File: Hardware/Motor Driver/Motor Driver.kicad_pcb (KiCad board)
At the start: 2 copper layers, 65 x 85 mm, 9 parts, among them J1 Conn_01x02, J2 Conn_01x02, J3 Conn_01x04, J4 Conn_01x04, J5 Conn_01x06, J6 Conn_01x06, J7 Conn_01x02

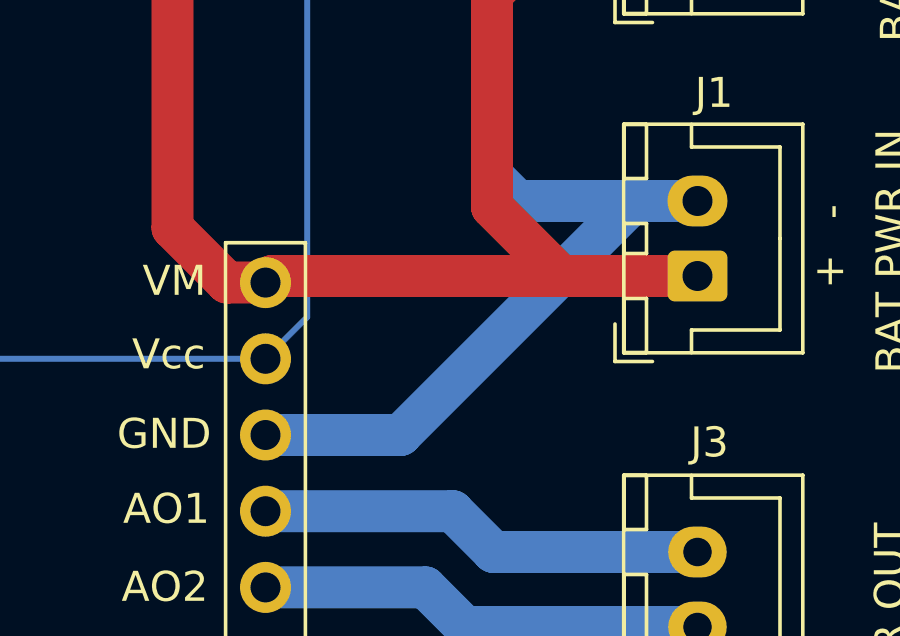
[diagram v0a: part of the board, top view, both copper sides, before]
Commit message: Updated battery input traces on the PCB.
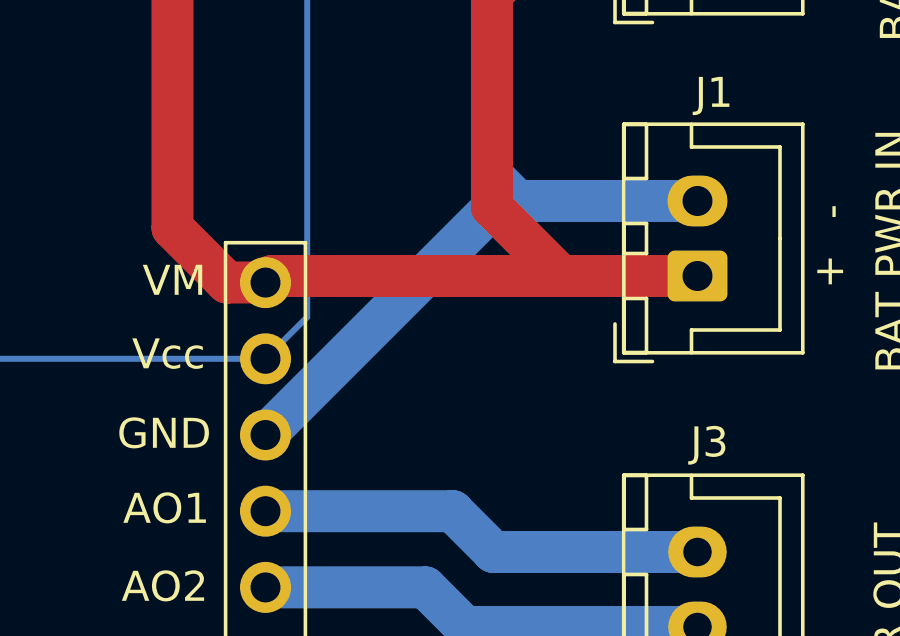
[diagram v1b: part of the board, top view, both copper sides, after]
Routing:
- net Net-(J1-Pin_2): track 71.3 -> 67.4 mm
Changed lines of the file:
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@@
+	)
+	(segment
+		(start 149.1 101.5)
+		(end 148.5 101.5)
+		(width 1.4)
+		(layer "B.Cu")
+		(net 2)
 	)
 	(segment
@@
 	(segment
 		(start 153 101.5)
-		(end 145.2 109.3)
-		(width 1.4)
-		(layer "B.Cu")
-		(net 2)
-	)
-	(segment
-		(start 153 101.5)
 		(end 149.1 101.5)
 		(width 1.4)
@@
 	)
 	(segment
-		(start 145.2 109.3)
+		(start 148.5 101.5)
 		(end 140.7 109.3)
 		(width 1.4)

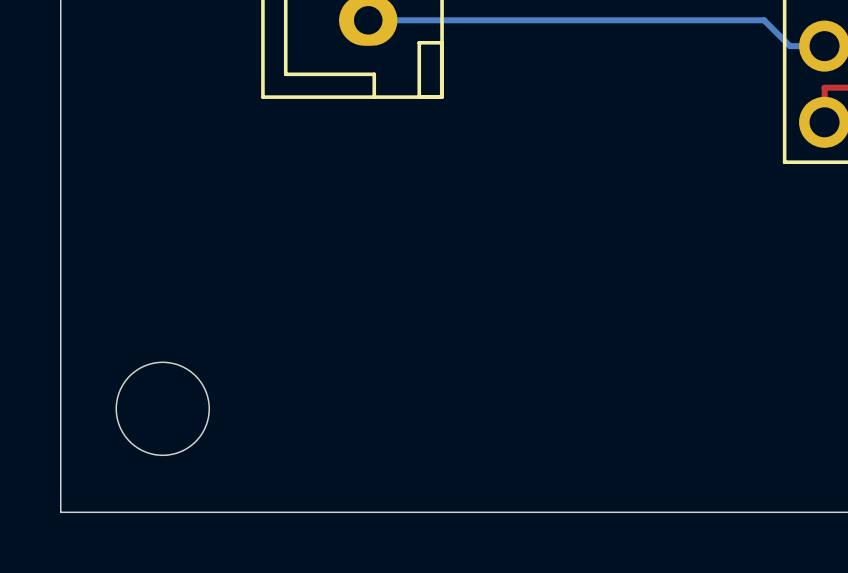
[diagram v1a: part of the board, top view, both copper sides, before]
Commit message: Added 86 logo to the front silkscreen, and designed by on the back silkscreen.
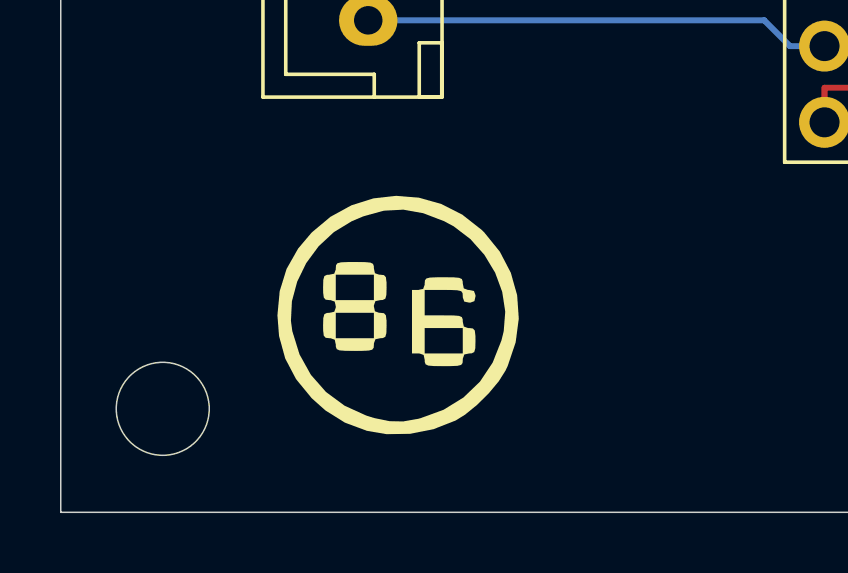
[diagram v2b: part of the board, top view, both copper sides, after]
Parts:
- added G***: LOGO, motor driver:86Carrera_logo, F.Cu at (111.2, 128.3)
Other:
- board text added: "Designed by 86 Carrera"
- board text added: "https://github.com/rallen911/Mecanum-Robot.git"
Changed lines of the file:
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@@
+		)
+	)
+	(footprint "motor driver:86Carrera_logo"
+		(layer "F.Cu")
+		(at 111.2 128.35)
+		(property "Reference" "G***"
+			(at 0 0 0)
+			(layer "F.SilkS")
+			(hide yes)
+			(effects
+				(font
+					(size 1.5 1.5)
+					(thickness 0.3)
+				)
+			)
+		)
+		(property "Value" "LOGO"
+			(at 0.75 0 0)
+			(layer "F.SilkS")
+			(hide yes)
+			(effects
+				(font
+					(size 1.5 1.5)
+					(thickness 0.3)
+				)
+			)
+		)
+		(property "Footprint" "motor driver:86Carrera_logo"
+			(at 0 0 0)
+			(layer "F.Fab")
+			(hide yes)
+			(effects
+				(font
+					(size 1.27 1.27)
+					(thickness 0.15)
+				)
+			)
+		)
+		(property "Datasheet" ""
+			(at 0 0 0)
+			(layer "F.Fab")
+			(hide yes)
+			(effects
+				(font
+					(size 1.27 1.27)
+					(thickness 0.15)
+				)
+			)
+		)
+		(property "Description" ""
+			(at 0 0 0)
+			(layer "F.Fab")
+			(hide yes)
+			(effects
+				(font
+					(size 1.27 1.27)
+					(thickness 0.15)
+				)
+			)
+		)
+		(attr board_only exclude_from_pos_files exclude_from_bom)
+		(fp_poly
+			(pts
+				(xy 0.741449 -3.837598) (xy 1.482138 -3.62887) (xy 2.183203 -3.273207) (xy 2.824011 -2.77061) (xy 2.918917 -2.677222)
+				(xy 3.435795 -2.039142) (xy 3.801361 -1.337024) (xy 4.012987 -0.587865) (xy 4.068047 0.19134) (xy 3.963912 0.983595)
+				(xy 3.697956 1.771902) (xy 3.629392 1.918851) (xy 3.39942 2.285007) (xy 3.066468 2.684218) (xy 2.676966 3.069849)
+				(xy 2.277342 3.395264) (xy 1.96754 3.588093) (xy 1.225425 3.879931) (xy 0.443616 4.033875) (xy -0.337761 4.045246)
+				(xy -0.993602 3.933478) (xy -1.726458 3.660945) (xy -2.378504 3.253211) (xy -2.83425 2.846555) (xy -3.355997 2.211121)
+				(xy -3.717833 1.522776) (xy -3.923203 0.773189) (xy -3.962943 0.267619) (xy -3.52724 0.267619) (xy -3.480628 0.613609)
+				(xy -3.240019 1.387148) (xy -2.862468 2.065889) (xy -2.357867 2.639381) (xy -1.736105 3.097172)
+				(xy -1.007073 3.42881) (xy -0.739602 3.510145) (xy -0.238038 3.612434) (xy 0.215249 3.620456) (xy 0.708559 3.534454)
+				(xy 0.787967 3.514372) (xy 1.558689 3.233457) (xy 2.222954 2.824461) (xy 2.772103 2.296427) (xy 3.197477 1.6584)
+				(xy 3.490417 0.919422) (xy 3.565295 0.613609) (xy 3.616431 -0.036276) (xy 3.516639 -0.695096) (xy 3.280488 -1.335951)
+				(xy 2.922548 -1.931941) (xy 2.457388 -2.456165) (xy 1.89958 -2.881723) (xy 1.578429 -3.054768) (xy 0.878026 -3.321907)
+				(xy 0.218948 -3.438093) (xy -0.431958 -3.403279) (xy -1.107846 -3.217421) (xy -1.502943 -3.050473)
+				(xy -2.094889 -2.690372) (xy -2.60493 -2.216201) (xy -3.018124 -1.655638) (xy -3.319534 -1.036361)
+				(xy -3.494219 -0.386049) (xy -3.52724 0.267619) (xy -3.962943 0.267619) (xy -3.977324 0.084667)
+				(xy -3.901699 -0.723266) (xy -3.672528 -1.462908) (xy -3.286363 -2.142588) (xy -2.83425 -2.677222)
+				(xy -2.204916 -3.203166) (xy -1.512047 -3.582176) (xy -0.776276 -3.814251) (xy -0.018233 -3.899392)
+			)
+			(stroke
+				(width 0)
+				(type solid)
+			)
+			(fill solid)
+			(layer "F.SilkS")
+		)
+		(fp_poly
+			(pts
+				(xy 1.889321 -1.182696) (xy 2.078649 -1.166856) (xy 2.169985 -1.125924) (xy 2.198999 -1.048011)
+				(xy 2.201333 -0.973667) (xy 2.236303 -0.812545) (xy 2.373993 -0.762894) (xy 2.413 -0.762) (xy 2.574122 -0.727031)
+				(xy 2.623773 -0.58934) (xy 2.624667 -0.550333) (xy 2.589697 -0.389212) (xy 2.452007 -0.339561) (xy 2.413 -0.338667)
+				(xy 2.251878 -0.373636) (xy 2.202227 -0.511327) (xy 2.201333 -0.550333) (xy 2.193419 -0.657996)
+				(xy 2.145899 -0.721105) (xy 2.023105 -0.751551) (xy 1.789367 -0.761222) (xy 1.566333 -0.762) (xy 0.931333 -0.762)
+				(xy 0.931333 -0.338667) (xy 0.931333 0.084667) (xy 1.566333 0.084667) (xy 1.889321 0.087304) (xy 2.078649 0.103144)
+				(xy 2.169985 0.144076) (xy 2.198999 0.221989) (xy 2.201333 0.296333) (xy 2.236303 0.457455) (xy 2.373993 0.507106)
+				(xy 2.413 0.508) (xy 2.538622 0.521725) (xy 2.601292 0.59177) (xy 2.622661 0.76144) (xy 2.624667 0.931333)
+				(xy 2.617804 1.182577) (xy 2.582781 1.307917) (xy 2.497947 1.350656) (xy 2.413 1.354667) (xy 2.251878 1.389636)
+				(xy 2.202227 1.527326) (xy 2.201333 1.566333) (xy 2.193419 1.673996) (xy 2.145899 1.737105) (xy 2.023105 1.76755)
+				(xy 1.789367 1.777222) (xy 1.566333 1.778) (xy 1.243346 1.775362) (xy 1.054018 1.759522) (xy 0.962681 1.71859)
+				(xy 0.933667 1.640678) (xy 0.931333 1.566333) (xy 0.896364 1.405211) (xy 0.758673 1.35556) (xy 0.719667 1.354667)
+				(xy 0.508 1.354667) (xy 0.508 0.931333) (xy 0.931333 0.931333) (xy 0.931333 1.354667) (xy 1.566333 1.354667)
+				(xy 2.201333 1.354667) (xy 2.201333 0.931333) (xy 2.201333 0.508) (xy 1.566333 0.508) (xy 0.931333 0.508)
+				(xy 0.931333 0.931333) (xy 0.508 0.931333) (xy 0.508 0.296333) (xy 0.508 -0.762) (xy 0.719667 -0.762)
+				(xy 0.880788 -0.79697) (xy 0.930439 -0.93466) (xy 0.931333 -0.973667) (xy 0.939247 -1.081329) (xy 0.986767 -1.144439)
+				(xy 1.109562 -1.174884) (xy 1.3433 -1.184555) (xy 1.566333 -1.185333)
+			)
+			(stroke
+				(width 0)
+				(type solid)
+			)
+			(fill solid)
+			(layer "F.SilkS")
+		)
+		(fp_poly
+			(pts
+				(xy -1.074013 -1.690696) (xy -0.884685 -1.674856) (xy -0.793348 -1.633924) (xy -0.764334 -1.556011)
+				(xy -0.762 -1.481667) (xy -0.727031 -1.320545) (xy -0.58934 -1.270894) (xy -0.550333 -1.27) (xy -0.424711 -1.256275)
+				(xy -0.362042 -1.18623) (xy -0.340672 -1.01656) (xy -0.338667 -0.846667) (xy -0.345529 -0.595423)
+				(xy -0.380552 -0.470083) (xy -0.465387 -0.427344) (xy -0.550333 -0.423333) (xy -0.711455 -0.388364)
+				(xy -0.761106 -0.250674) (xy -0.762 -0.211667) (xy -0.727031 -0.050545) (xy -0.58934 -0.000894)
+				(xy -0.550333 0) (xy -0.424711 0.013725) (xy -0.362042 0.08377) (xy -0.340672 0.25344) (xy -0.338667 0.423333)
+				(xy -0.345529 0.674577) (xy -0.380552 0.799917) (xy -0.465387 0.842656) (xy -0.550333 0.846667)
+				(xy -0.711455 0.881636) (xy -0.761106 1.019326) (xy -0.762 1.058333) (xy -0.769914 1.165996) (xy -0.817434 1.229105)
+				(xy -0.940229 1.25955) (xy -1.173967 1.269222) (xy -1.397 1.27) (xy -1.719988 1.267362) (xy -1.909316 1.251522)
+				(xy -2.000652 1.21059) (xy -2.029666 1.132678) (xy -2.032 1.058333) (xy -2.06697 0.897211) (xy -2.20466 0.84756)
+				(xy -2.243667 0.846667) (xy -2.369289 0.832941) (xy -2.431959 0.762896) (xy -2.453328 0.593227)
+				(xy -2.455333 0.423333) (xy -2.032 0.423333) (xy -2.032 0.846667) (xy -1.397 0.846667) (xy -0.762 0.846667)
+				(xy -0.762 0.423333) (xy -0.762 0) (xy -1.397 0) (xy -2.032 0) (xy -2.032 0.423333) (xy -2.455333 0.423333)
+				(xy -2.448471 0.172089) (xy -2.413448 0.046749) (xy -2.328614 0.00401) (xy -2.243667 0) (xy -2.082545 -0.03497)
+				(xy -2.032894 -0.17266) (xy -2.032 -0.211667) (xy -2.06697 -0.372789) (xy -2.20466 -0.42244) (xy -2.243667 -0.423333)
+				(xy -2.369289 -0.437059) (xy -2.431959 -0.507104) (xy -2.453328 -0.676773) (xy -2.455333 -0.846667)
+				(xy -2.032 -0.846667) (xy -2.032 -0.423333) (xy -1.397 -0.423333) (xy -0.762 -0.423333) (xy -0.762 -0.846667)
+				(xy -0.762 -1.27) (xy -1.397 -1.27) (xy -2.032 -1.27) (xy -2.032 -0.846667) (xy -2.455333 -0.846667)
+				(xy -2.448471 -1.097911) (xy -2.413448 -1.223251) (xy -2.328614 -1.26599) (xy -2.243667 -1.27) (xy -2.082545 -1.30497)
+				(xy -2.032894 -1.44266) (xy -2.032 -1.481667) (xy -2.024086 -1.589329) (xy -1.976566 -1.652439)
+				(xy -1.853772 -1.682884) (xy -1.620034 -1.692555) (xy -1.397 -1.693333)
+			)
+			(stroke
+				(width 0)
+				(type solid)
+			)
+			(fill solid)
+			(layer "F.SilkS")
 		)
 	)
@@
 		)
 		(fp_text user "${REFERENCE}"
+			(at 15.24 8.89 90)
+			(layer "F.Fab")
+			(effects
+				(font
+					(size 1 1)
+					(thickness 0.15)
+				)
+			)
+		)
+		(fp_text user "${REFERENCE}"
 			(at 0 8.89 90)
-			(layer "F.Fab")
-			(effects
-				(font
-					(size 1 1)
-					(thickness 0.15)
-				)
-			)
-		)
-		(fp_text user "${REFERENCE}"
-			(at 15.24 8.89 90)
 			(layer "F.Fab")
 			(effects
@@
 		(layer "Edge.Cuts")
 	)
+	(gr_text "https://github.com/rallen911/Mecanum-Robot.git"
+		(at 152.1 56.05 0)
+		(layer "B.SilkS")
+		(effects
+			(font
+				(size 1 1)
+				(thickness 0.1)
+			)
+			(justify left bottom mirror)
+		)
+	)
+	(gr_text "Designed by 86 Carrera"
+		(at 151.25 131.35 0)
+		(layer "B.SilkS")
+		(effects
+			(font
+				(size 2 2)
+				(thickness 0.4)
+				(bold yes)
+			)
+			(justify left bottom mirror)
+		)
+	)
 	(gr_text "BO1"

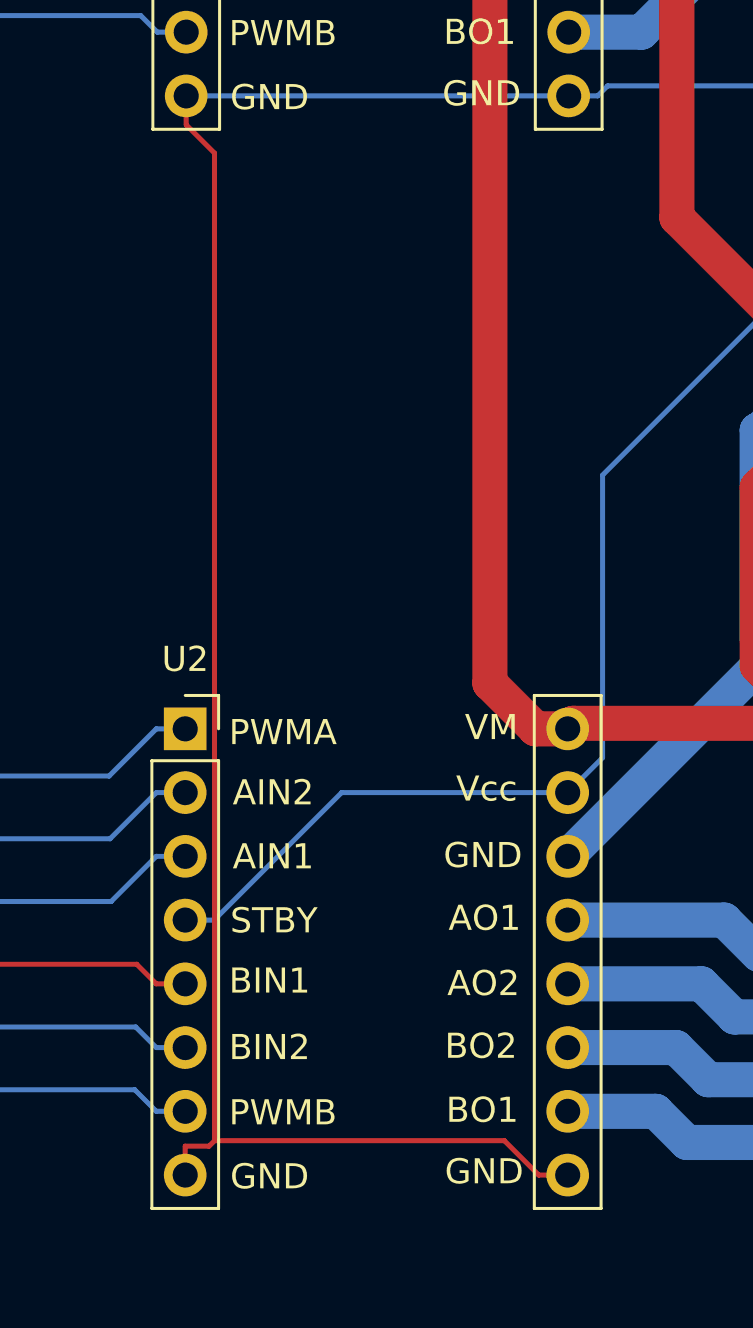
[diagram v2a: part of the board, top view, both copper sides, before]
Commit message: Fixed digital power trace routing around U2 pin 8.
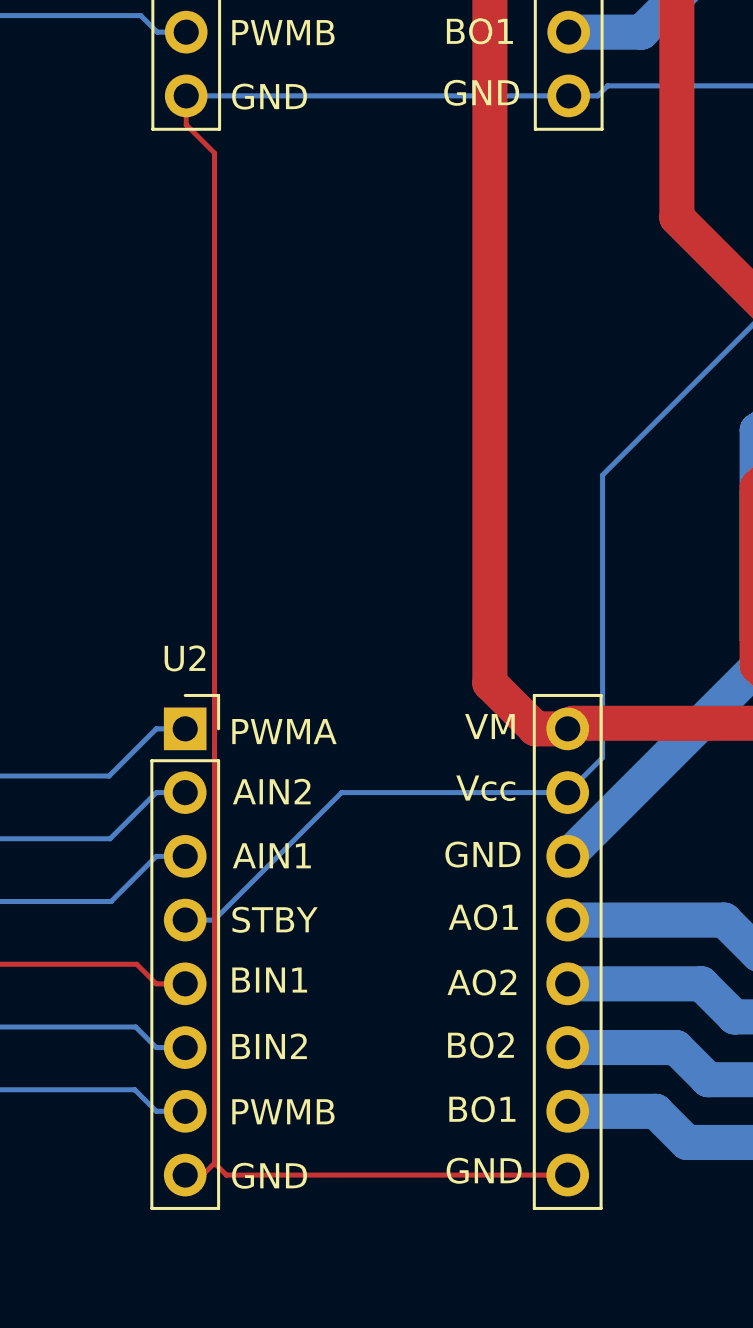
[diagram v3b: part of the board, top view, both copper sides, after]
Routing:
- net Net-(J2-Pin_2): track 88.9 -> 88.4 mm
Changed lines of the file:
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@@
 	)
 	(segment
-		(start 125.46 120.8483)
-		(end 126.408 120.8483)
+		(start 126.6272 81.2789)
+		(end 126.6272 121.5272)
 		(width 0.2)
 		(layer "F.Cu")
@@
 	)
 	(segment
-		(start 126.6272 120.6291)
-		(end 138.1774 120.6291)
+		(start 126.6272 121.5272)
+		(end 126.1544 122)
 		(width 0.2)
 		(layer "F.Cu")
@@
 	)
 	(segment
-		(start 125.46 122)
-		(end 125.46 120.8483)
+		(start 125.5 80.1517)
+		(end 126.6272 81.2789)
 		(width 0.2)
 		(layer "F.Cu")
@@
 	)
 	(segment
-		(start 138.1774 120.6291)
-		(end 139.5483 122)
-		(width 0.2)
-		(layer "F.Cu")
-		(net 4)
-	)
-	(segment
-		(start 126.6272 81.2789)
-		(end 126.6272 120.6291)
-		(width 0.2)
-		(layer "F.Cu")
-		(net 4)
-	)
-	(segment
-		(start 126.408 120.8483)
-		(end 126.6272 120.6291)
+		(start 126.1544 122)
+		(end 125.46 122)
 		(width 0.2)
 		(layer "F.Cu")
@@
 	)
 	(segment
-		(start 140.7 122)
-		(end 139.5483 122)
+		(start 126.6272 121.5272)
+		(end 127.1 122)
 		(width 0.2)
 		(layer "F.Cu")
@@
 	)
 	(segment
-		(start 125.5 80.1517)
-		(end 126.6272 81.2789)
+		(start 140.7 122)
+		(end 127.1 122)
 		(width 0.2)
 		(layer "F.Cu")

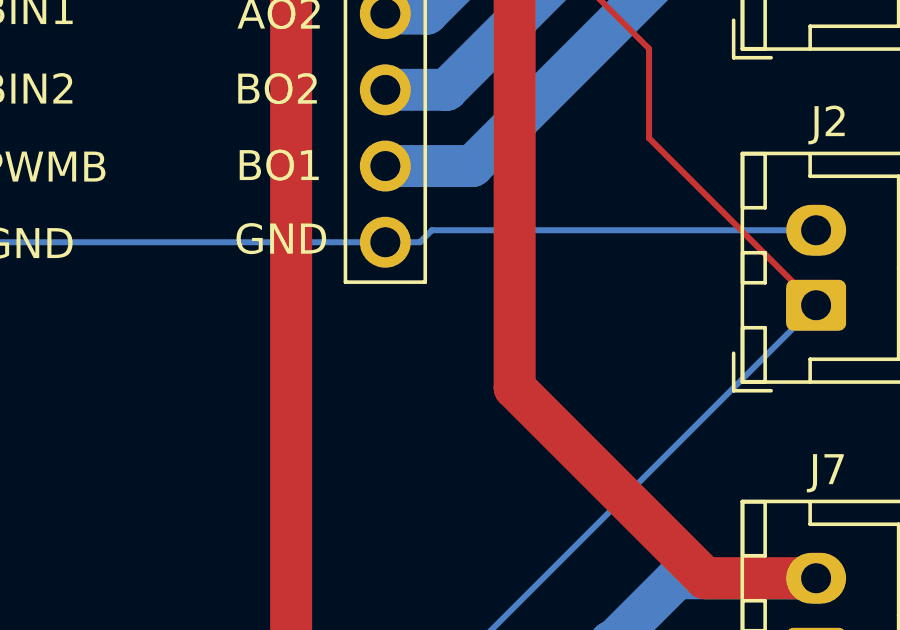
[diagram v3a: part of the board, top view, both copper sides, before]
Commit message: Connected the battery and buck converter grounds, because isolation wasn't needed in this application.
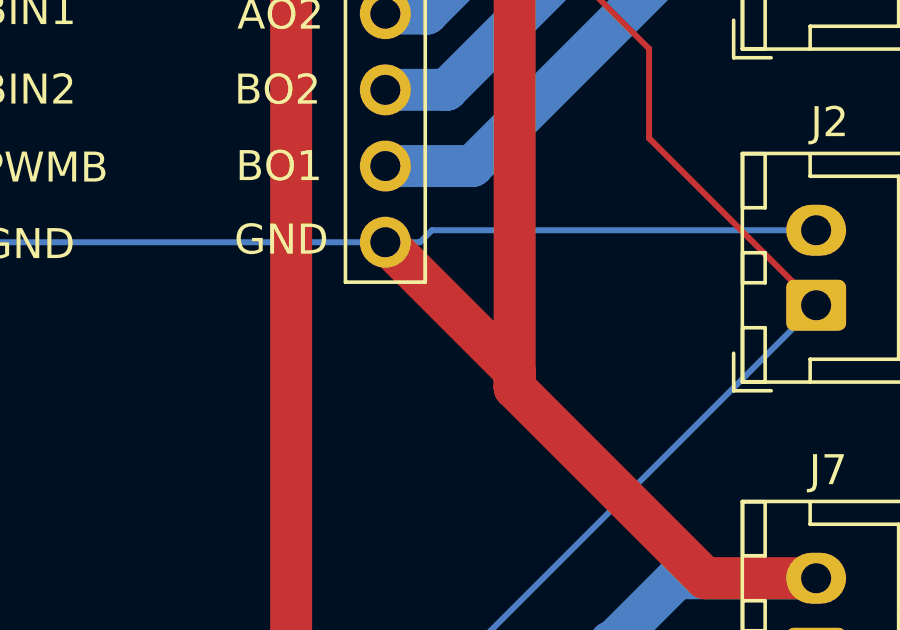
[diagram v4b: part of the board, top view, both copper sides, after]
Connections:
- J2 pad 2: Net-(J2-Pin_2) -> Net-(J1-Pin_2)
- U1 pad 8: Net-(J2-Pin_2) -> Net-(J1-Pin_2)
- U1 pad 9: Net-(J2-Pin_2) -> Net-(J1-Pin_2)
- U2 pad 8: Net-(J2-Pin_2) -> Net-(J1-Pin_2)
- U2 pad 9: Net-(J2-Pin_2) -> Net-(J1-Pin_2)
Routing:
- net Net-(J1-Pin_2): track 67.4 -> 162.5 mm
- net Net-(J2-Pin_2): track 88.4 -> 0.00 mm
